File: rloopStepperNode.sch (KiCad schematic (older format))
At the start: 0 parts

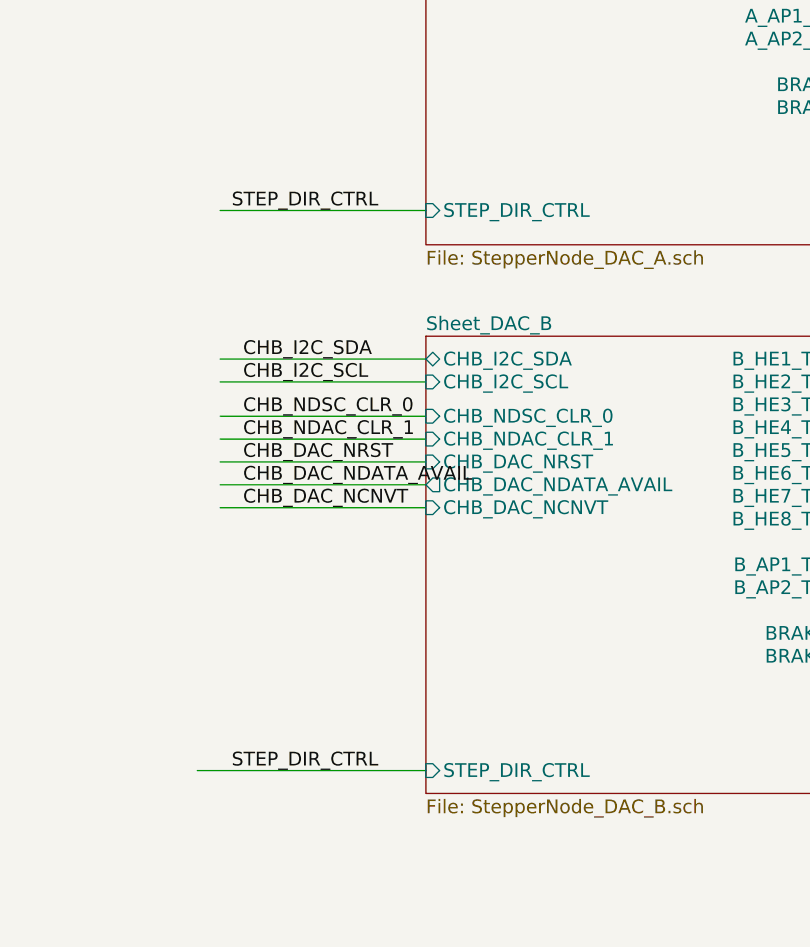
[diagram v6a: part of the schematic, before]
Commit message: Fix further ERC warnings
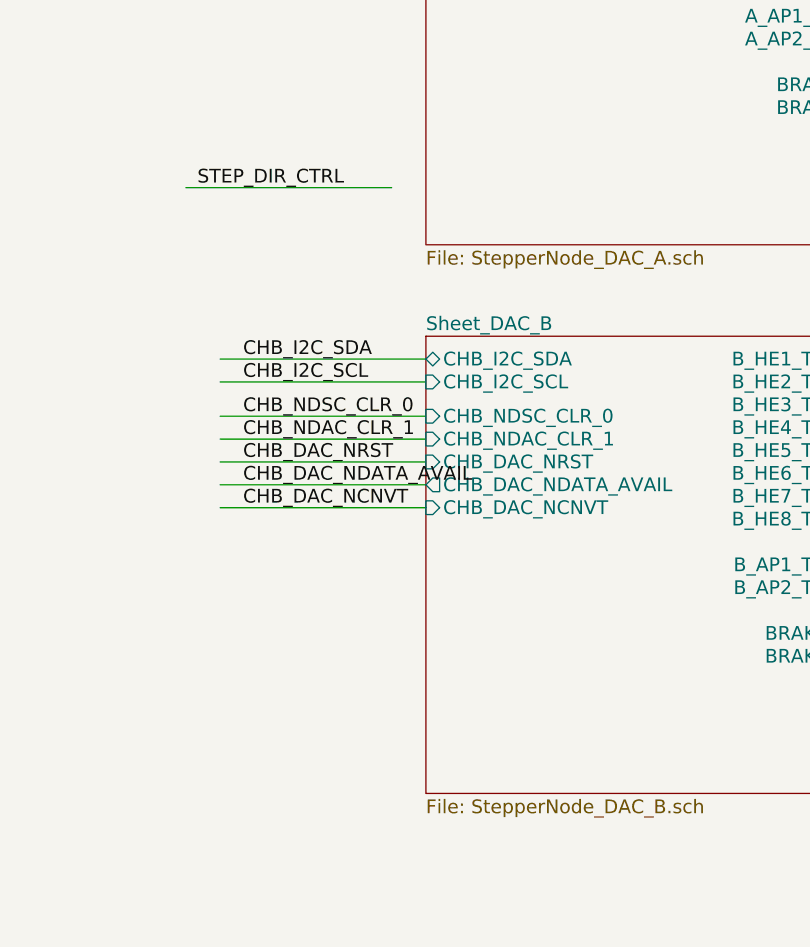
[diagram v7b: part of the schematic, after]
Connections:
- wire segments 150 -> 149
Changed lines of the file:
@@
 BRAKE2_MLP_3V
 Wire Wire Line
-	5650 5650 6550 5650
-Text Label 5700 5650 0    60   ~ 0
-STEP_DIR_CTRL
-Wire Wire Line
-	5550 8100 6550 8100
-Text Label 5700 8100 0    60   ~ 0
+	5500 5550 6400 5550
+Text Label 5550 5550 0    60   ~ 0
 STEP_DIR_CTRL
 Wire Wire Line
@@
 F8 "B_HE7_THROTTLE" O R 8700 6900 60
 F9 "B_HE8_THROTTLE" O R 8700 7000 60
-F10 "STEP_DIR_CTRL" I L 6550 8100 60
 F11 "CHB_I2C_SDA" B L 6550 6300 60
 F12 "CHB_I2C_SCL" I L 6550 6400 60
@@
 F15 "A_HE7_THROTTLE" O R 8750 4550 60
 F16 "A_HE8_THROTTLE" O R 8750 4650 60
-F17 "STEP_DIR_CTRL" I L 6550 5650 60
 F18 "A_AP1_THROTTLE" O R 8750 4800 60
 F19 "A_AP2_THROTTLE" O R 8750 4900 60
